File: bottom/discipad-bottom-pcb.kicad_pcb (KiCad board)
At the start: 2 copper layers, 76.3 x 122.8 mm, 11 parts

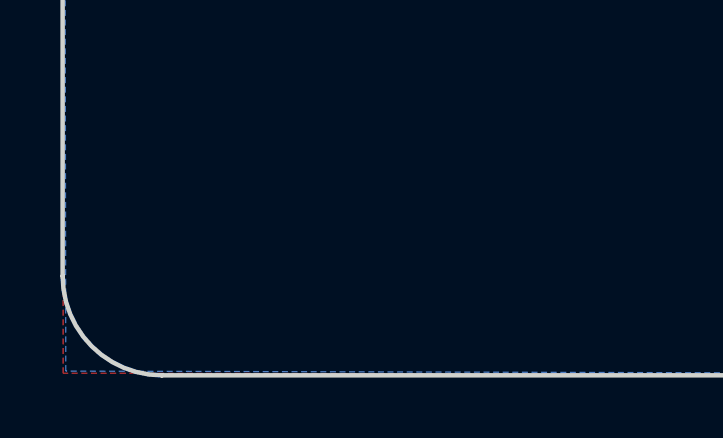
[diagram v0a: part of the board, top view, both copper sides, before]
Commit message: Update bottom with plated logo and JLCPCB order placeholder
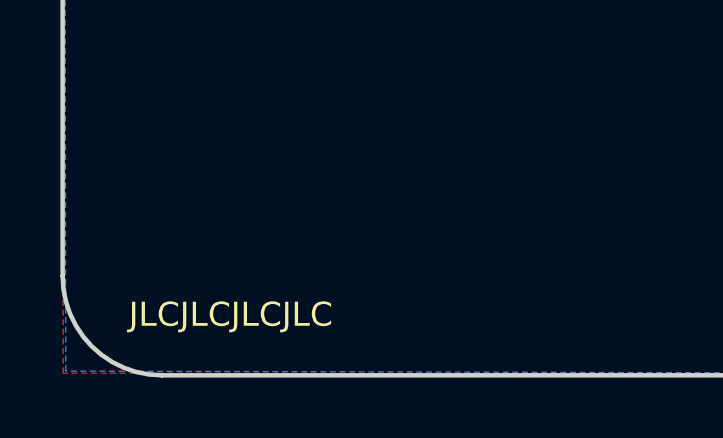
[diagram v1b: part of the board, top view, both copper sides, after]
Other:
- board text added: "JLCJLCJLCJLC"

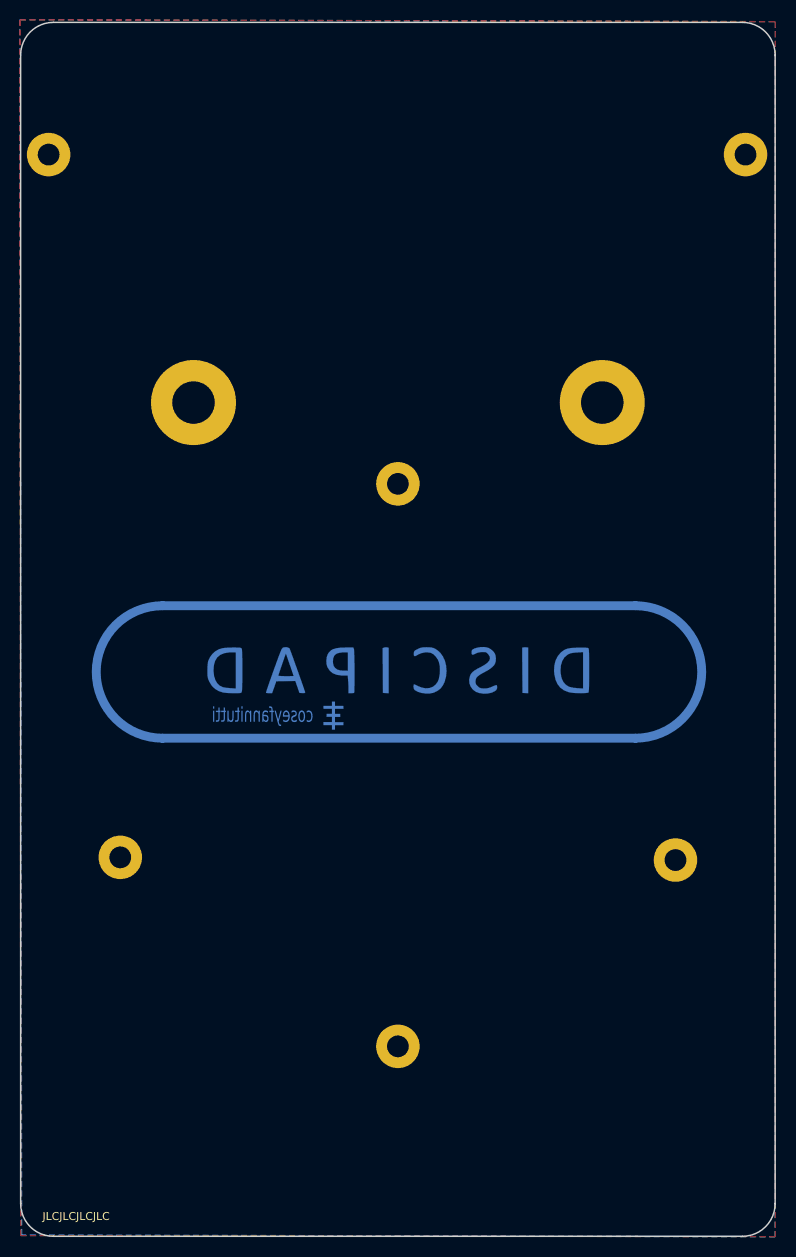
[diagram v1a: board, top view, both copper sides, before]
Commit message: Bottom RevC: move cone feet holes further apart for better stability
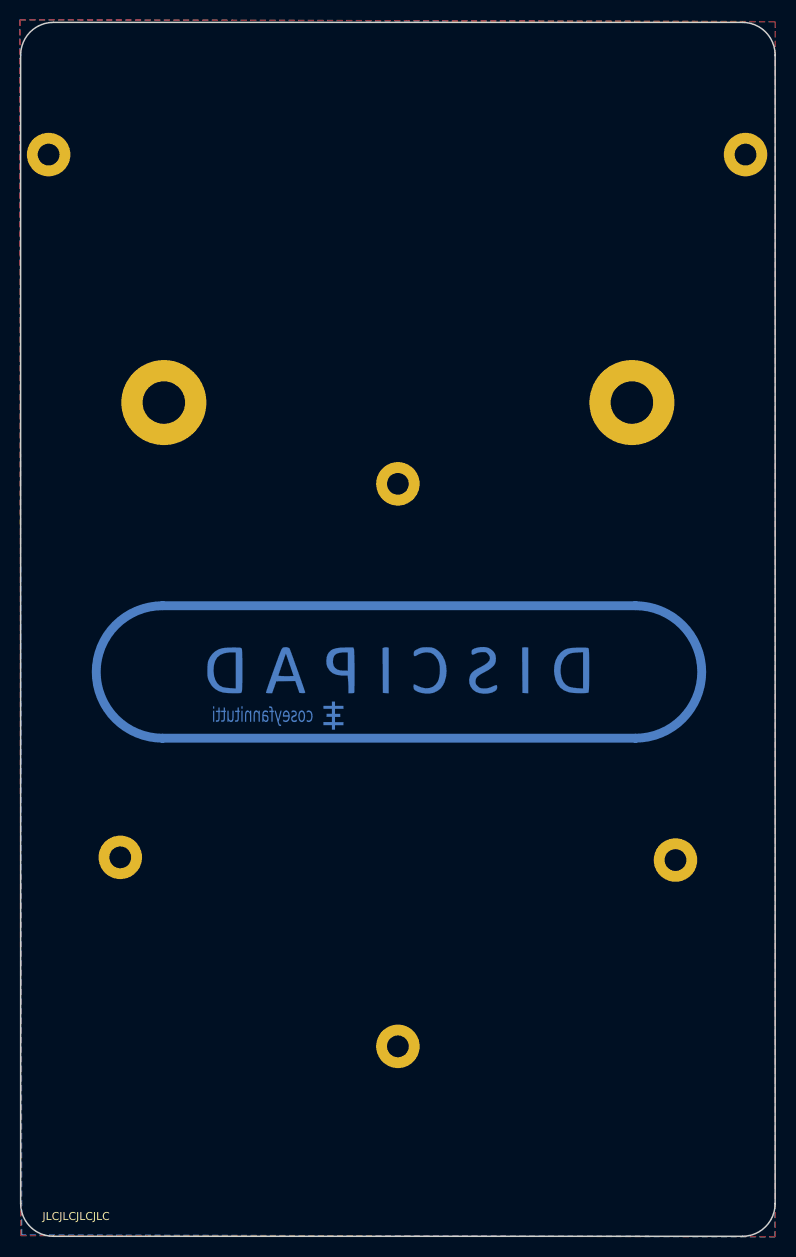
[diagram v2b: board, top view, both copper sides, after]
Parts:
- moved REF** 3.00 mm to (167.5, 53.6)
- moved REF** 3.00 mm to (120.2, 53.6)
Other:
- net class Default removed
